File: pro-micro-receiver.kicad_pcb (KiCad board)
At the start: 4 copper layers, 63.7 x 19.5 mm, 40 parts, among them J1 USB_A_PLUG, J2 Conn_01x04, SW1 SW_Push, U1 TLV740P, U2 ATmega32U4-M, U3 YJ-14015, Y1 16MHz

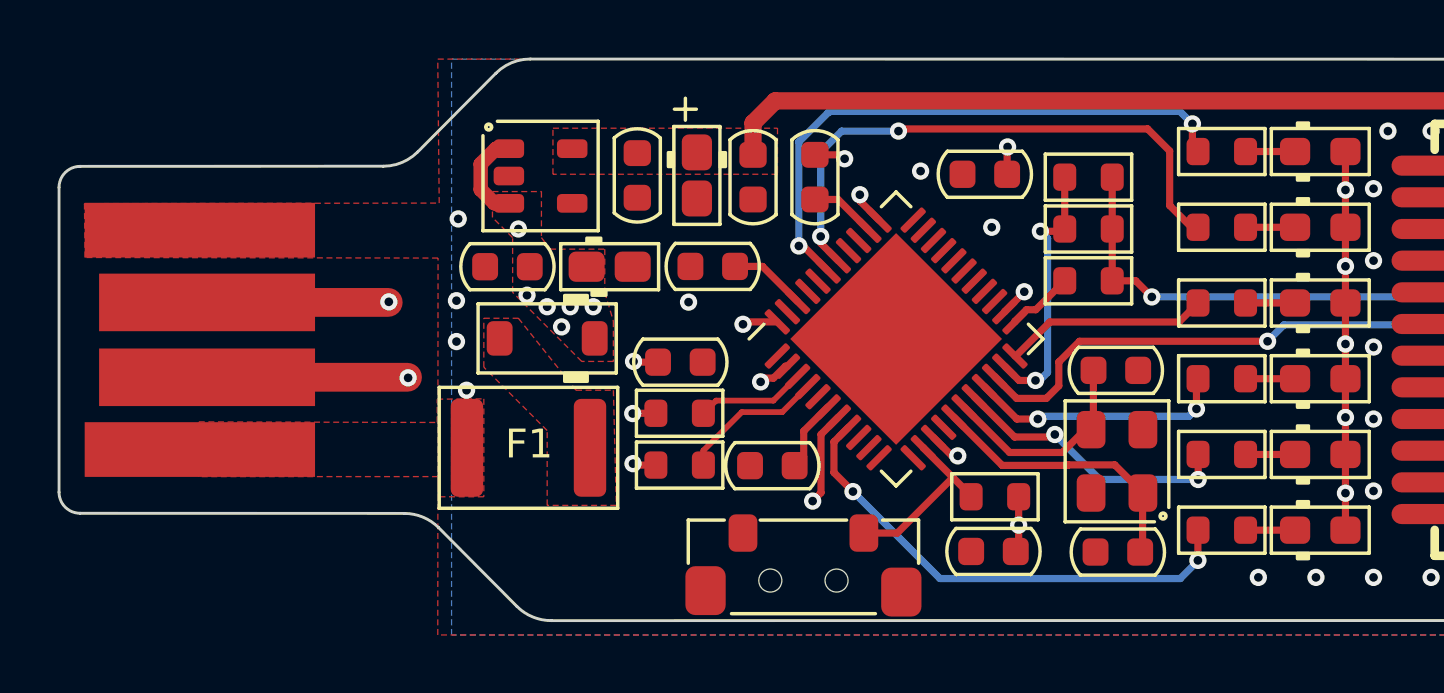
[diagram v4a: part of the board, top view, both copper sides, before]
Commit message: Adding testpoints to PCB
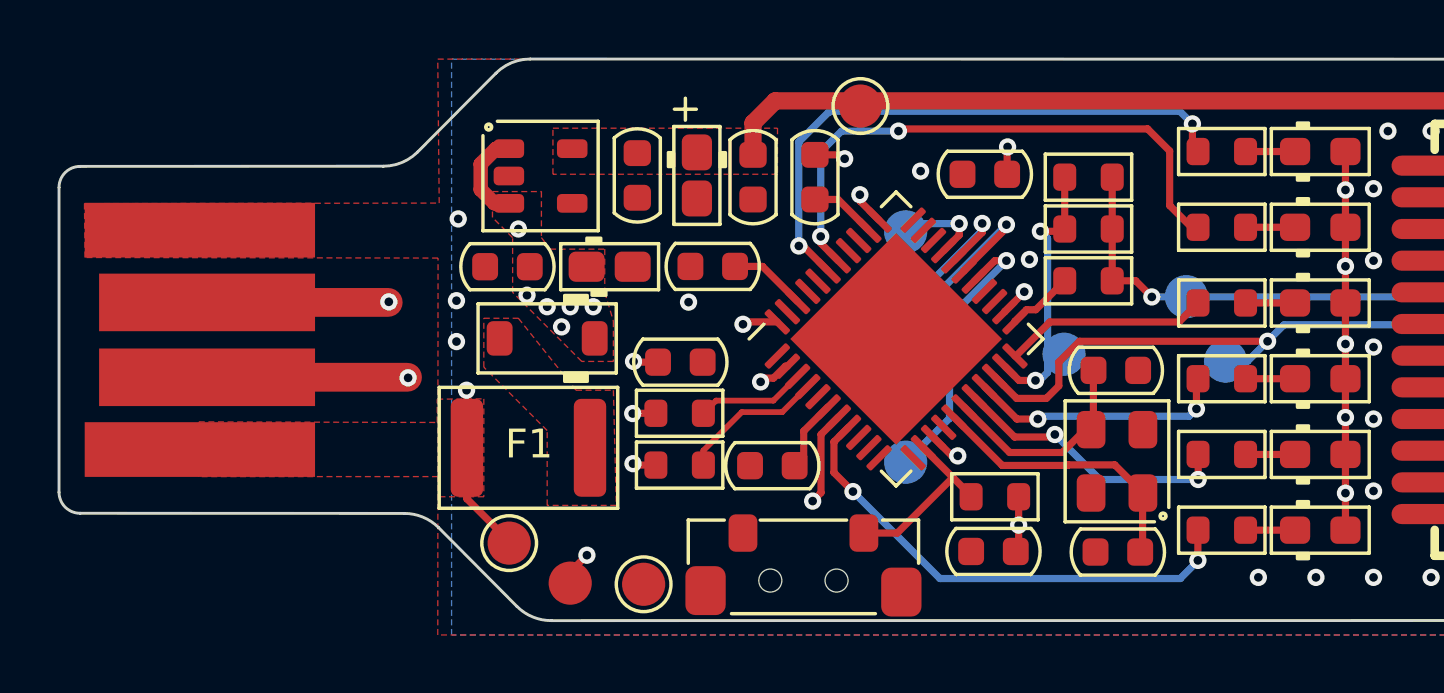
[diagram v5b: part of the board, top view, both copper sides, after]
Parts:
- added TP1: TestPoint, TestPoint:TestPoint_Pad_D1.5mm, F.Cu at (78.6, 82.2)
- added TP11: TestPoint, TestPoint:TestPoint_Pad_D1.5mm, B.Cu at (100.0, 72.2)
- added TP12: TestPoint, TestPoint:TestPoint_Pad_D1.5mm, B.Cu at (101.4, 74.5)
- added TP13: TestPoint, TestPoint:TestPoint_Pad_D1.5mm, B.Cu at (95.8, 74.2)
- added TP2: TestPoint, TestPoint:TestPoint_Pad_D1.5mm, F.Cu at (81.2, 82.2)
- added TP3: TestPoint, TestPoint:TestPoint_Pad_D1.5mm, F.Cu at (88.7, 65.6)
- added TP4: TestPoint, TestPoint:TestPoint_Pad_D1.5mm, B.Cu at (90.2, 75.3)
- added TP5: TestPoint, TestPoint:TestPoint_Pad_D1.5mm, B.Cu at (90.2, 72.7)
- added TP6: TestPoint, TestPoint:TestPoint_Pad_D1.5mm, B.Cu at (90.2, 70.0)
- added TP7: TestPoint, TestPoint:TestPoint_Pad_D1.5mm, B.Cu at (90.2, 78.0)
- added TP8: TestPoint, TestPoint:TestPoint_Pad_D1.5mm, F.Cu at (76.5, 80.8)
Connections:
- U2 pad 27: unconnected-(U2-Pad27) -> PD7
- U2 pad 28: unconnected-(U2-Pad28) -> PB4
- U2 pad 29: unconnected-(U2-Pad29) -> PB5
- U2 pad 30: unconnected-(U2-Pad30) -> PB6
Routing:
- net PD7: track 0.00 -> 9.86 mm, vias 0 -> 1
- net PB4: track 0.00 -> 9.25 mm, vias 0 -> 1
- net PB5: track 0.00 -> 5.77 mm, vias 0 -> 1
- net UVCC: track 26.6 -> 30.5 mm
- net PB6: track 0.00 -> 3.14 mm, vias 0 -> 1
- net RXI: track 32.2 -> 34.0 mm
- net VCC: track 24.9 -> 26.1 mm, vias 18 -> 19

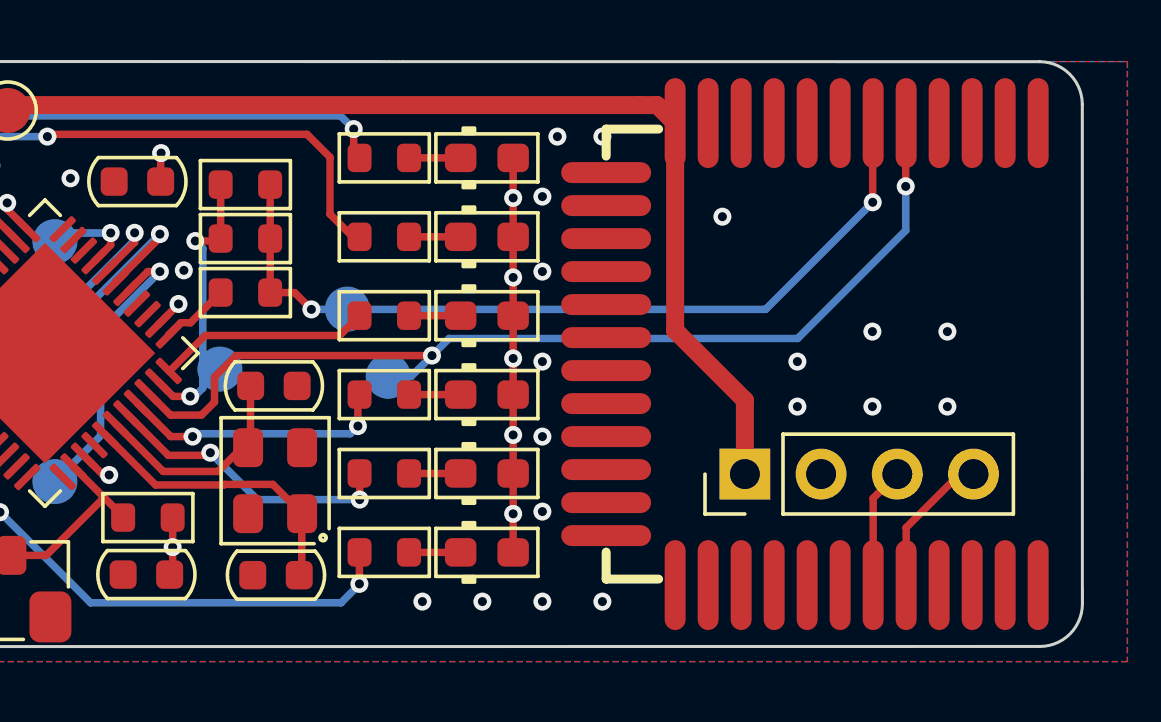
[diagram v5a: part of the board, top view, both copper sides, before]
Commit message: Adding flags for testpoints
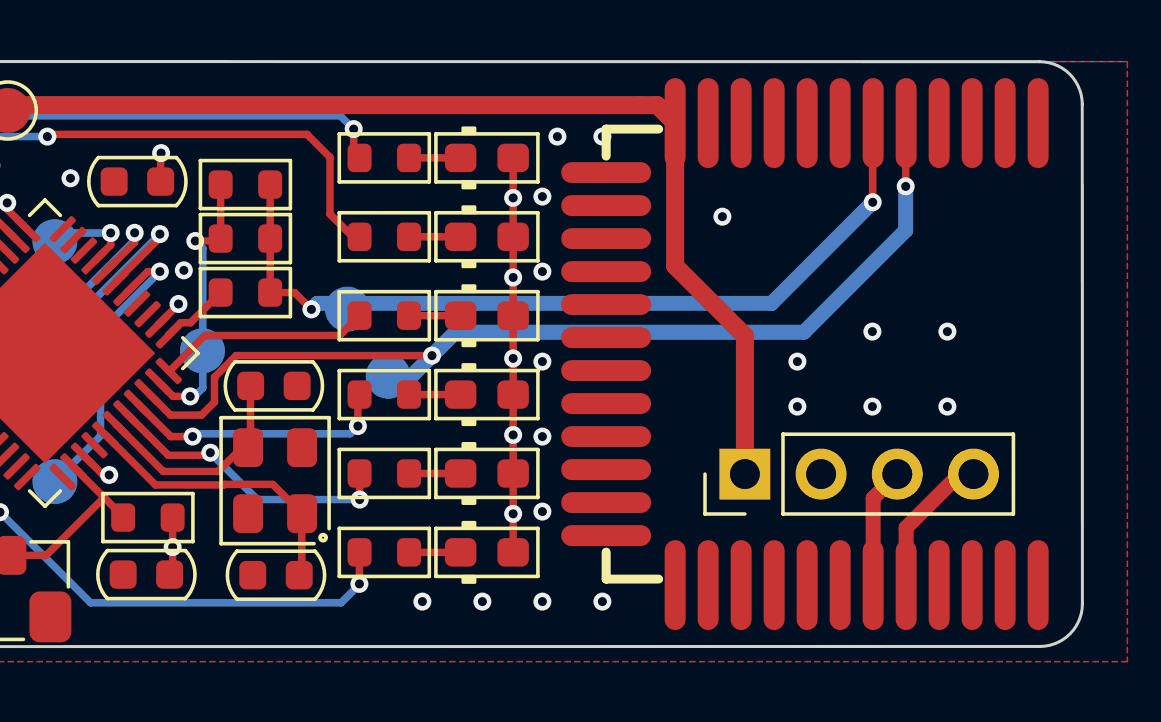
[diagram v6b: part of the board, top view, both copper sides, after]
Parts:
- added kibuzzard-63ACD5DB: G***, kibuzzard-63ACD5DB, B.Cu at (86.5, 70.0)
- added kibuzzard-63ACD5FF: G***, kibuzzard-63ACD5FF, B.Cu at (86.4, 72.7)
- added kibuzzard-63ACD615: G***, kibuzzard-63ACD615, B.Cu at (86.4, 75.3)
- added kibuzzard-63ACD627: G***, kibuzzard-63ACD627, B.Cu at (86.5, 78.0)
- added kibuzzard-63ACD667: G***, kibuzzard-63ACD667, B.Cu at (106.1, 74.6)
- added kibuzzard-63ACD680: G***, kibuzzard-63ACD680, B.Cu at (106.6, 72.2)
- added kibuzzard-63ACD69E: G***, kibuzzard-63ACD69E, B.Cu at (95.2, 71.2)
- moved TP13 0.84 mm to (95.2, 73.6)

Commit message: Small fixes on the PCB
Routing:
- net GND: vias 24 -> 32

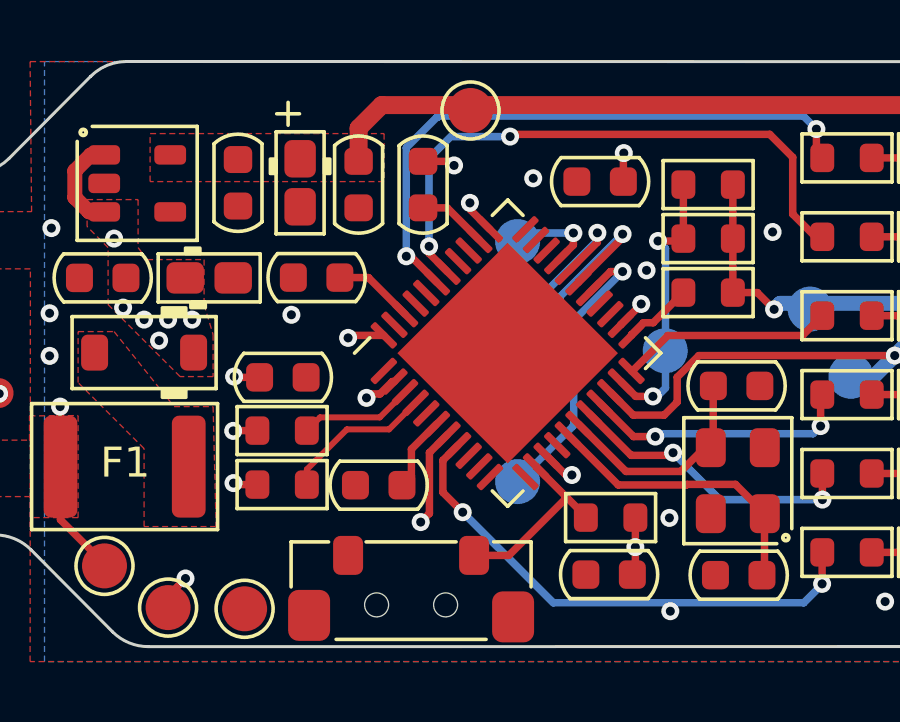
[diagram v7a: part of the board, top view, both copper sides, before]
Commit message: Adding labels to +3V3 and GND testpoints
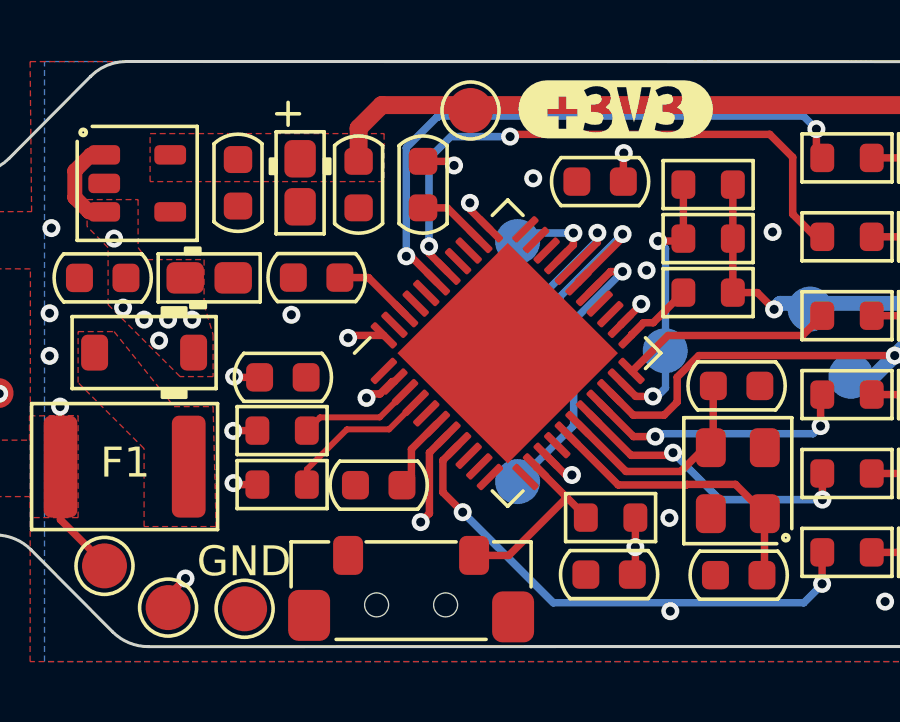
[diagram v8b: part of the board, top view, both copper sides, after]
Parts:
- added kibuzzard-63BC8742: G***, kibuzzard-63BC8742, F.Cu at (93.5, 65.6)
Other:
- board text added: "GND"
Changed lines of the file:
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@@
     )
+  )
+  (footprint "kibuzzard-63BC8742" (layer "F.Cu")
+    (at 93.52 65.59)
+    (descr "Converted using: scripting")
+    (tags "svg2mod")
+    (attr board_only exclude_from_pos_files exclude_from_bom)
+    (fp_text reference "kibuzzard-63BC8742" (at 0 -0.968089) (layer "F.SilkS") hide
+      (effects (font (size 0.000254 0.000254) (thickness 0.000003)))
+    )
+    (fp_text value "G***" (at 0 0.968089) (layer "F.SilkS") hide
+      (effects (font (size 0.000254 0.000254) (thickness 0.000003)))
+    )
+    (fp_poly (pts
+        (xy -2.275284 -0.967581)
+        (xy -2.275284 -0.007144)
+        (xy -1.901428 -0.007144)
+        (xy -1.901428 -0.421481)
+        (xy -1.649016 -0.421481)
+        (xy -1.649016 -0.007144)
+        (xy -1.275159 -0.007144)
+        (xy -1.275159 0.233363)
+        (xy -1.649016 0.233363)
+        (xy -1.082278 0.688181)
+        (xy -1.025128 0.442913)
+        (xy -0.883444 0.492919)
+        (xy -0.787896 0.512564)
+        (xy -0.675084 0.519113)
+        (xy -0.54739 0.503039)
+        (xy -0.464344 0.454819)
+        (xy -0.403622 0.295275)
+        (xy -0.426839 0.196155)
+        (xy -0.496491 0.132159)
+        (xy -0.601861 0.097334)
+        (xy -0.732234 0.085725)
+        (xy -0.822722 0.085725)
+        (xy -0.822722 -0.157163)
+        (xy -0.713184 -0.157163)
+        (xy -0.622697 -0.166688)
+        (xy -0.541734 -0.197644)
+        (xy -0.483394 -0.254794)
+        (xy -0.460772 -0.345281)
+        (xy -0.509588 -0.472678)
+        (xy -0.644128 -0.519113)
+        (xy -0.809625 -0.491728)
+        (xy -0.951309 -0.423863)
+        (xy -1.056084 -0.638175)
+        (xy -0.885825 -0.725091)
+        (xy -0.773013 -0.75813)
+        (xy -0.646509 -0.769144)
+        (xy -0.530721 -0.761405)
+        (xy -0.431006 -0.738188)
+        (xy -0.279797 -0.651272)
+        (xy -0.191691 -0.519113)
+        (xy -0.163116 -0.354806)
+        (xy -0.213122 -0.185738)
+        (xy -0.346472 -0.061913)
+        (xy -0.244971 -0.002977)
+        (xy -0.169069 0.078581)
+        (xy -0.121741 0.18038)
+        (xy -0.105966 0.300038)
+        (xy -0.139303 0.488156)
+        (xy 0.453628 0.738188)
+        (xy 0.394692 0.563166)
+        (xy 0.332184 0.366713)
+        (xy 0.290116 0.228732)
+        (xy 0.249634 0.091017)
+        (xy 0.210741 -0.046434)
+        (xy 0.173964 -0.18124)
+        (xy 0.139832 -0.311018)
+        (xy 0.108347 -0.435769)
+        (xy 0.069056 -0.602456)
+        (xy 0.041672 -0.735806)
+        (xy 0.351234 -0.735806)
+        (xy 0.369094 -0.612279)
+        (xy 0.394097 -0.470297)
+        (xy 0.42416 -0.316706)
+        (xy 0.4572 -0.158353)
+        (xy 0.492919 0.001191)
+        (xy 0.531019 0.158353)
+        (xy 0.570012 0.306288)
+        (xy 0.608409 0.43815)
+        (xy 0.646509 0.308074)
+        (xy 0.684609 0.160734)
+        (xy 0.721519 0.003572)
+        (xy 0.756047 -0.155972)
+        (xy 0.788194 -0.314623)
+        (xy 0.817959 -0.469106)
+        (xy 0.844153 -0.611981)
+        (xy 0.865584 -0.735806)
+        (xy 1.172766 -0.735806)
+        (xy 1.140916 -0.584597)
+        (xy 1.102519 -0.416719)
+        (xy 1.05787 -0.236041)
+        (xy 1.007269 -0.046434)
+        (xy 0.970359 0.083741)
+        (xy 0.931069 0.215503)
+        (xy 0.889397 0.348853)
+        (xy 0.846005 0.481542)
+        (xy 0.801555 0.61132)
+        (xy 1.372791 0.714375)
+        (xy 1.298972 0.688181)
+        (xy 1.356122 0.442913)
+        (xy 1.497806 0.492919)
+        (xy 1.593354 0.512564)
+        (xy 1.706166 0.519113)
+        (xy 1.83386 0.503039)
+        (xy 1.916906 0.454819)
+        (xy 1.977628 0.295275)
+        (xy 1.954411 0.196155)
+        (xy 1.884759 0.132159)
+        (xy 1.779389 0.097334)
+        (xy 1.649016 0.085725)
+        (xy 1.558528 0.085725)
+        (xy 1.558528 -0.157163)
+        (xy 1.668066 -0.157163)
+        (xy 1.758553 -0.166688)
+        (xy 1.839516 -0.197644)
+        (xy 1.897856 -0.254794)
+        (xy 1.920478 -0.345281)
+        (xy 1.871663 -0.472678)
+        (xy 1.737122 -0.519113)
+        (xy 1.571625 -0.491728)
+        (xy 1.429941 -0.423863)
+        (xy 1.325166 -0.638175)
+        (xy 1.495425 -0.725091)
+        (xy 1.608237 -0.75813)
+        (xy 1.734741 -0.769144)
+        (xy 1.850529 -0.761405)
+        (xy 1.950244 -0.738188)
+        (xy 2.101453 -0.651272)
+        (xy 2.189559 -0.519113)
+        (xy 2.218134 -0.354806)
+        (xy 2.168128 -0.185738)
+        (xy 2.034778 -0.061913)
+        (xy 2.136279 -0.002977)
+        (xy 2.212181 0.078581)
+        (xy 2.259509 0.18038)
+        (xy 2.275284 0.300038)
+        (xy 2.241947 0.488156)
+        (xy 2.139553 0.636984)
+        (xy 2.060972 0.692944)
+        (xy 1.963341 0.734616)
+        (xy 1.846064 0.760512)
+        (xy 1.708547 0.769144)
+        (xy 1.593056 0.760809)
+        (xy 1.476375 0.740569)
+        (xy 1.372791 0.714375)
+        (xy 0.801555 0.61132)
+        (xy 0.756047 0.738188)
+        (xy 0.453628 0.738188)
+        (xy -0.139303 0.488156)
+        (xy -0.241697 0.636984)
+        (xy -0.320278 0.692944)
+        (xy -0.417909 0.734616)
+        (xy -0.535186 0.760512)
+        (xy -0.672703 0.769144)
+        (xy -0.788194 0.760809)
+        (xy -0.904875 0.740569)
+        (xy -1.008459 0.714375)
+        (xy -1.082278 0.688181)
+        (xy -1.649016 0.233363)
+        (xy -1.649016 0.6477)
+        (xy -1.901428 0.6477)
+        (xy -1.901428 0.233363)
+        (xy -2.275284 0.233363)
+        (xy -2.275284 -0.007144)
+        (xy -2.275284 -0.967581)
+        (xy -2.275483 -0.967581)
+        (xy -2.464249 -0.948989)
+        (xy -2.64576 -0.893929)
+        (xy -2.813042 -0.804514)
+        (xy -2.959666 -0.684183)
+        (xy -3.079997 -0.537559)
+        (xy -3.169411 -0.370277)
+        (xy -3.224472 -0.188766)
+        (xy -3.243064 0)
+        (xy -3.224472 0.188766)
+        (xy -3.169411 0.370277)
+        (xy -3.079997 0.537559)
+        (xy -2.959666 0.684183)
+        (xy -2.813042 0.804514)
+        (xy -2.64576 0.893929)
+        (xy -2.464249 0.948989)
+        (xy -2.275483 0.967581)
+        (xy -2.275284 0.967581)
+        (xy 2.275284 0.967581)
+        (xy 2.275483 0.967581)
+        (xy 2.464249 0.948989)
+        (xy 2.64576 0.893929)
+        (xy 2.813042 0.804514)
+        (xy 2.959666 0.684183)
+        (xy 3.079997 0.537559)
+        (xy 3.169411 0.370277)
+        (xy 3.224472 0.188766)
+        (xy 3.243064 0)
+        (xy 3.224472 -0.188766)
+        (xy 3.169411 -0.370277)
+        (xy 3.079997 -0.537559)
+        (xy 2.959666 -0.684183)
+        (xy 2.813042 -0.804514)
+        (xy 2.64576 -0.893929)
+        (xy 2.464249 -0.948989)
+        (xy 2.275483 -0.967581)
+        (xy 2.275284 -0.967581)
+        (xy -2.275284 -0.967581)
+      ) (layer "F.SilkS") (width 0) (fill solid))
   )
   (footprint "Diode_SMD_AKL:D_0603_1608Metric_Pad1.05x0.95mm" (layer "F.Cu")
@@
   (gr_line (start 99.54 81.21) (end 106.4 81.21) (layer "User.1") (width 0.15))
   (gr_line (start 99.54 66.39) (end 106.38 66.39) (layer "User.1") (width 0.15))
+  (gr_text "GND" (at 81.13 80.66) (layer "F.SilkS")
+    (effects (font (size 1 1) (thickness 0.15)))
+  )
   (dimension (type orthogonal) (layer "User.1")
     (pts (xy 72.8375 67.72) (xy 128.65 68.25))
